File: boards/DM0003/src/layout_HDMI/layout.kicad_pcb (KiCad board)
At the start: 2 copper layers, 4 parts, among them IC1 STMPS2151STR, J1 ?

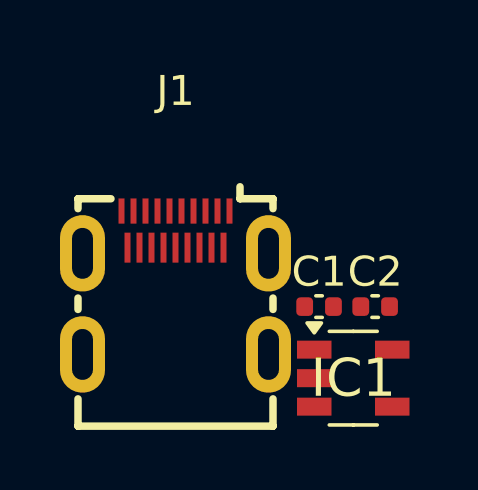
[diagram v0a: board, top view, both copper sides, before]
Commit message: Sync layouts (#61)
* Sync reference design layouts

* Remove stale properties

* Update board layouts
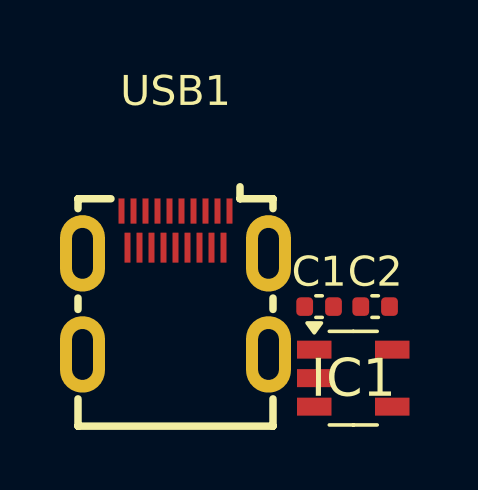
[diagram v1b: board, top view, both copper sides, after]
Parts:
- C1, C2: value 100nF 16V X7R -> GCM155R71H104KE02D
- USB1: renamed from J1; value ? -> 685119248123
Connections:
- net fault renamed FAULT
- net hdmi_5v renamed HDMI_5V
- net io_5v renamed 5V
- net nc renamed HDMI_Connector.NC_HDMI-101S_UTILITY
- C1 pad 2: io_gnd -> GND
- C2 pad 2: io_gnd -> GND
- IC1 pad 2: io_gnd -> GND
- USB1 pad 10: io_gnd -> GND
- USB1 pad 13: io_gnd -> GND
- USB1 pad 16: io_gnd -> GND
- USB1 pad 20: (no net) -> GND
- USB1 pad 4: io_gnd -> GND
- USB1 pad 7: io_gnd -> GND
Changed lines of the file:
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@@
 	)
 	(net 0 "")
-	(net 1 "hdmi_5v")
-	(net 2 "nc")
+	(net 1 "HDMI_5V")
+	(net 2 "HDMI_Connector.NC_HDMI-101S_UTILITY")
 	(net 3 "HDMI_C_D2_N")
 	(net 4 "HDMI_C_D1_P")
 	(net 5 "HDMI_C_D1_N")
 	(net 6 "HDMI_C_HPD")
-	(net 7 "io_5v")
-	(net 8 "io_gnd")
+	(net 7 "5V")
+	(net 8 "GND")
 	(net 9 "HDMI_C_CLK_P")
 	(net 10 "HDMI_C_D0_N")
@@
 	(net 12 "HDMI_C_D0_P")
 	(net 13 "HDMI_C_D2_P")
-	(net 14 "fault")
+	(net 14 "FAULT")
 	(net 15 "HDMI_C_CLK_N")
 	(net 16 "HDMI_C_CEC")
@@
 			(size 0.6 1.15)
 			(layers "F.Cu" "F.Mask" "F.Paste")
-			(net 1 "hdmi_5v")
+			(net 1 "HDMI_5V")
 		)
 		(pad "2" smd rect
@@
 			(size 0.6 1.15)
 			(layers "F.Cu" "F.Mask" "F.Paste")
-			(net 8 "io_gnd")
+			(net 8 "GND")
 		)
 		(pad "3" smd rect
@@
 			(size 0.6 1.15)
 			(layers "F.Cu" "F.Mask" "F.Paste")
-			(net 14 "fault")
+			(net 14 "FAULT")
 		)
 		(pad "4" smd rect
@@
 			(size 0.6 1.15)
 			(layers "F.Cu" "F.Mask" "F.Paste")
-			(net 7 "io_5v")
+			(net 7 "5V")
 		)
 		(pad "5" smd rect
@@
 			(size 0.6 1.15)
 			(layers "F.Cu" "F.Mask" "F.Paste")
-			(net 7 "io_5v")
+			(net 7 "5V")
 		)
 		(embedded_fonts no)
@@
 			)
 		)
-		(property "Value" "100nF 16V X7R"
+		(property "Value" "GCM155R71H104KE02D"
 			(at 0 1.16 0)
 			(layer "F.Fab")
@@
 		)
 		(property "Dielectric" "X7R"
+			(at 0 0 0)
+			(layer "F.SilkS")
+			(hide yes)
+			(effects
+				(font
+					(size 1.27 1.27)
+					(thickness 0.15)
+				)
+			)
+		)
+		(property "Alternatives" "{\"mpn\": \"GCM155R71H104KE02J\", \"manufacturer\": \"Murata Electronics\"}"
+			(at 0 0 0)
+			(layer "F.SilkS")
+			(hide yes)
+			(effects
+				(font
+					(size 1.27 1.27)
+					(thickness 0.15)
+				)
+			)
+		)
+		(property "Manufacturer" "Murata Electronics"
+			(at 0 0 0)
+			(layer "F.SilkS")
+			(hide yes)
+			(effects
+				(font
+					(size 1.27 1.27)
+					(thickness 0.15)
+				)
+			)
+		)
+		(property "Matcher" "assign_house_capacitor"
+			(at 0 0 0)
+			(layer "F.SilkS")
+			(hide yes)
+			(effects
+				(font
+					(size 1.27 1.27)
+					(thickness 0.15)
+				)
+			)
+		)
+		(property "Mpn" "GCM155R71H104KE02D"
 			(at 0 0 0)
 			(layer "F.SilkS")
@@
 			(layers "F.Cu" "F.Mask" "F.Paste")
 			(roundrect_rratio 0.25)
-			(net 7 "io_5v")
+			(net 7 "5V")
 		)
 		(pad "2" smd roundrect
@@
 			(layers "F.Cu" "F.Mask" "F.Paste")
 			(roundrect_rratio 0.25)
-			(net 8 "io_gnd")
+			(net 8 "GND")
 		)
 		(embedded_fonts no)
@@
 			)
 		)
-		(property "Value" "100nF 16V X7R"
+		(property "Value" "GCM155R71H104KE02D"
 			(at 0 1.16 0)
 			(layer "F.Fab")
@@
 		)
 		(property "Dielectric" "X7R"
+			(at 0 0 0)
+			(layer "F.SilkS")
+			(hide yes)
+			(effects
+				(font
+					(size 1.27 1.27)
+					(thickness 0.15)
+				)
+			)
+		)
+		(property "Alternatives" "{\"mpn\": \"GCM155R71H104KE02J\", \"manufacturer\": \"Murata Electronics\"}"
+			(at 0 0 0)
+			(layer "F.SilkS")
+			(hide yes)
+			(effects
+				(font
+					(size 1.27 1.27)
+					(thickness 0.15)
+				)
+			)
+		)
+		(property "Manufacturer" "Murata Electronics"
+			(at 0 0 0)
+			(layer "F.SilkS")
+			(hide yes)
+			(effects
+				(font
+					(size 1.27 1.27)
+					(thickness 0.15)
+				)
+			)
+		)
+		(property "Matcher" "assign_house_capacitor"
+			(at 0 0 0)
+			(layer "F.SilkS")
+			(hide yes)
+			(effects
+				(font
+					(size 1.27 1.27)
+					(thickness 0.15)
+				)
+			)
+		)
+		(property "Mpn" "GCM155R71H104KE02D"
 			(at 0 0 0)
 			(layer "F.SilkS")
@@
 			(layers "F.Cu" "F.Mask" "F.Paste")
 			(roundrect_rratio 0.25)
-			(net 1 "hdmi_5v")
+			(net 1 "HDMI_5V")
 		)
 		(pad "2" smd roundrect
@@
 			(layers "F.Cu" "F.Mask" "F.Paste")
 			(roundrect_rratio 0.25)
-			(net 8 "io_gnd")
+			(net 8 "GND")
 		)
 		(embedded_fonts no)
@@
 		(layer "F.Cu")
 		(at 146.425 104.21)
-		(property "Reference" "J1"
+		(property "Reference" "USB1"
 			(at 0 -6.39 0)
 			(layer "F.SilkS")
@@
 			)
 		)
-		(property "Value" "?"
+		(property "Value" "685119248123"
 			(at 0 6.39 0)
 			(layer "F.Fab")
@@
 			)
 		)
-		(property "Datasheet" "http://pinoutguide.com/PortableDevices/micro_hdmi_type_d_pinout.shtml"
-			(at 0 0 0)
-			(layer "F.Fab")
-			(hide yes)
-			(effects
-				(font
-					(size 1.27 1.27)
-					(thickness 0.15)
-				)
-			)
-		)
-		(property "Description" "HDMI 1.4+ type D connector"
+		(property "Datasheet" "https://www.hdmi.org/sites/default/files/documents/HDMI_Specification_1.4_Final.pdf"
+			(at 0 0 0)
+			(layer "F.Fab")
+			(hide yes)
+			(effects
+				(font
+					(size 1.27 1.27)
+					(thickness 0.15)
+				)
+			)
+		)
+		(property "Description" "HDMI 1.0b compliant 1080p display port to HDMI 1.4a"
 			(at 0 0 0)
 			(layer "F.Fab")
@@
 			)
 		)
-		(property "Prefix" "J"
+		(property "Prefix" "USB"
+			(at 0 0 0)
+			(layer "F.SilkS")
+			(hide yes)
+			(effects
+				(font
+					(size 1.27 1.27)
+					(thickness 0.15)
+				)
+			)
+		)
+		(property "Lcsc Part" "C720620"
+			(at 0 0 0)
+			(layer "F.SilkS")
+			(hide yes)
+			(effects
+				(font
+					(size 1.27 1.27)
+					(thickness 0.15)
+				)
+			)
+		)
+		(property "Alternatives" "{\"mpn\": \"HDMI-101S\", \"manufacturer\": \"XUNPU\"},{\"mpn\": \"685119248123\", \"manufacturer\": \"W\\xfcrth Elektronik\"}"
+			(at 0 0 0)
+			(layer "F.SilkS")
+			(hide yes)
+			(effects
+				(font
+					(size 1.27 1.27)
+					(thickness 0.15)
+				)
+			)
+		)
+		(property "Manufacturer" "Würth Elektronik"
+			(at 0 0 0)
+			(layer "F.SilkS")
+			(hide yes)
+			(effects
+				(font
+					(size 1.27 1.27)
+					(thickness 0.15)
+				)
+			)
+		)
+		(property "Mpn" "685119248123"
 			(at 0 0 0)
 			(layer "F.SilkS")
@@
 			(size 0.2 1)
 			(layers "F.Cu" "F.Mask" "F.Paste")
-			(net 2 "nc")
+			(net 2 "HDMI_Connector.NC_HDMI-101S_UTILITY")
+			(pintype "no_connect")
 		)
 		(pad "3" smd rect
@@
 			(size 0.2 1)
 			(layers "F.Cu" "F.Mask" "F.Paste")
-			(net 8 "io_gnd")
+			(net 8 "GND")
 		)
 		(pad "5" smd rect
@@
 			(size 0.2 0.84)
 			(layers "F.Cu" "F.Mask" "F.Paste")
-			(net 8 "io_gnd")
+			(net 8 "GND")
 		)
 		(pad "8" smd rect
@@
 			(size 0.2 1)
 			(layers "F.Cu" "F.Mask" "F.Paste")
-			(net 8 "io_gnd")
+			(net 8 "GND")
 		)
 		(pad "11" smd rect
@@
 			(size 0.2 0.84)
 			(layers "F.Cu" "F.Mask" "F.Paste")
-			(net 8 "io_gnd")
+			(net 8 "GND")
 		)
 		(pad "14" smd rect
@@
 			(size 0.2 1)
 			(layers "F.Cu" "F.Mask" "F.Paste")
-			(net 8 "io_gnd")
+			(net 8 "GND")
 		)
 		(pad "17" smd rect
@@
 			(size 0.2 0.84)
 			(layers "F.Cu" "F.Mask" "F.Paste")
-			(net 1 "hdmi_5v")
+			(net 1 "HDMI_5V")
 		)
 		(pad "20" thru_hole oval
@@
 			(layers "*.Cu" "*.Mask")
 			(remove_unused_layers no)
+			(net 8 "GND")
 		)
 		(pad "20" thru_hole oval
@@
 	)
 	(group "Current_Limit_Switch"
-		(members "c8cc6591-4f23-433c-8e27-a96ab3681bc5" "d0f5ad37-35bf-4ff7-9e63-21d2f28fdecf"
-			"d15c858a-b50f-473f-904b-ca4e408fa4ac"
-		)
-	)
-	(group "Current_Limit_Switch.STMPS2151STR"
-		(members "abfae670-6087-4a7c-9f69-9a5e1f13d434")
+		(members "abfae670-6087-4a7c-9f69-9a5e1f13d434" "c8cc6591-4f23-433c-8e27-a96ab3681bc5"
+			"d0f5ad37-35bf-4ff7-9e63-21d2f28fdecf"
+		)
 	)
 	(embedded_fonts no)
